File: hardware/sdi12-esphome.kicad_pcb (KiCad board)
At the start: 2 copper layers, 92.8 x 74 mm, 32 parts, among them J0 Grounding, J1 SDI-12 A, J2 SDI-12 B, J3 SDI-12 C, J4 SDI-12 D, J5 GPIO21/22, J6 Rain Gauge, Q1 2N7002, U1 ESP32_NODEMCU, U2 74LVC1G125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

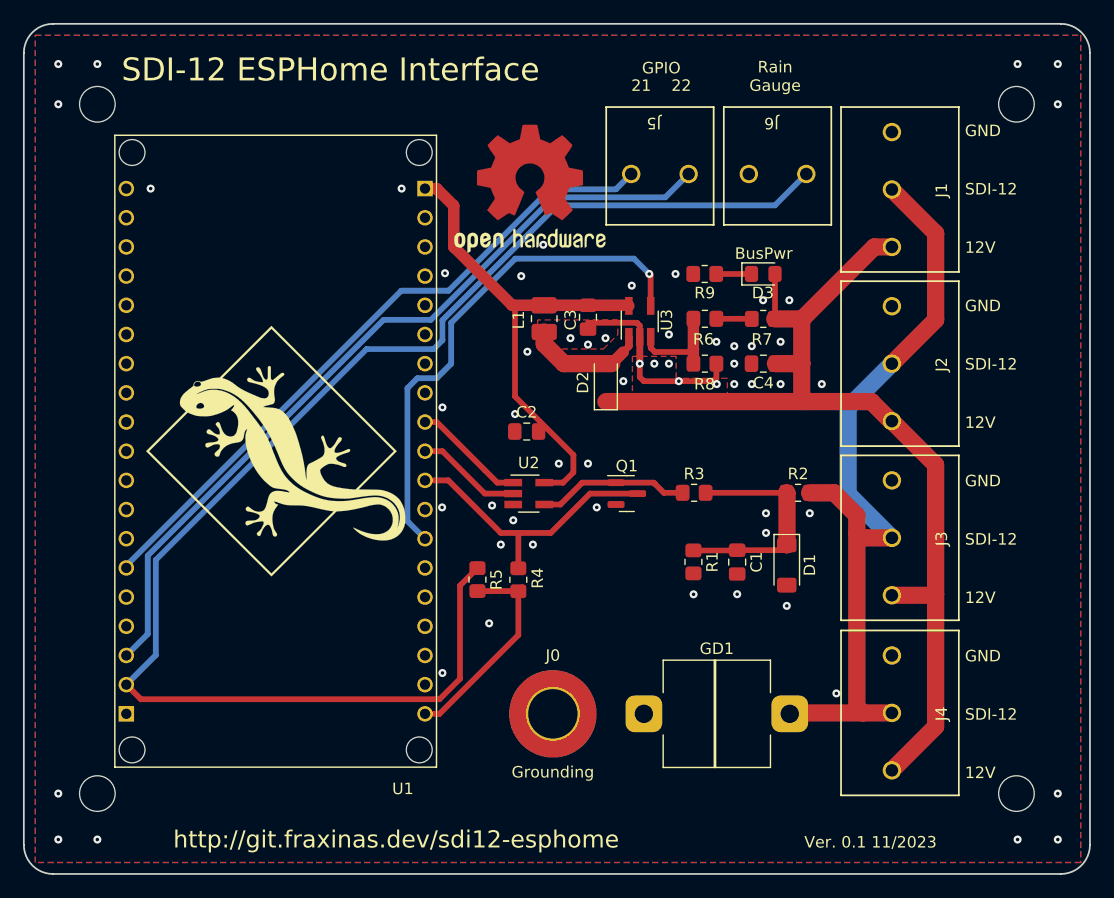
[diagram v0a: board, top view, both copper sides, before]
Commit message: board: Fix DRC errors (trace min spacing undercuts)
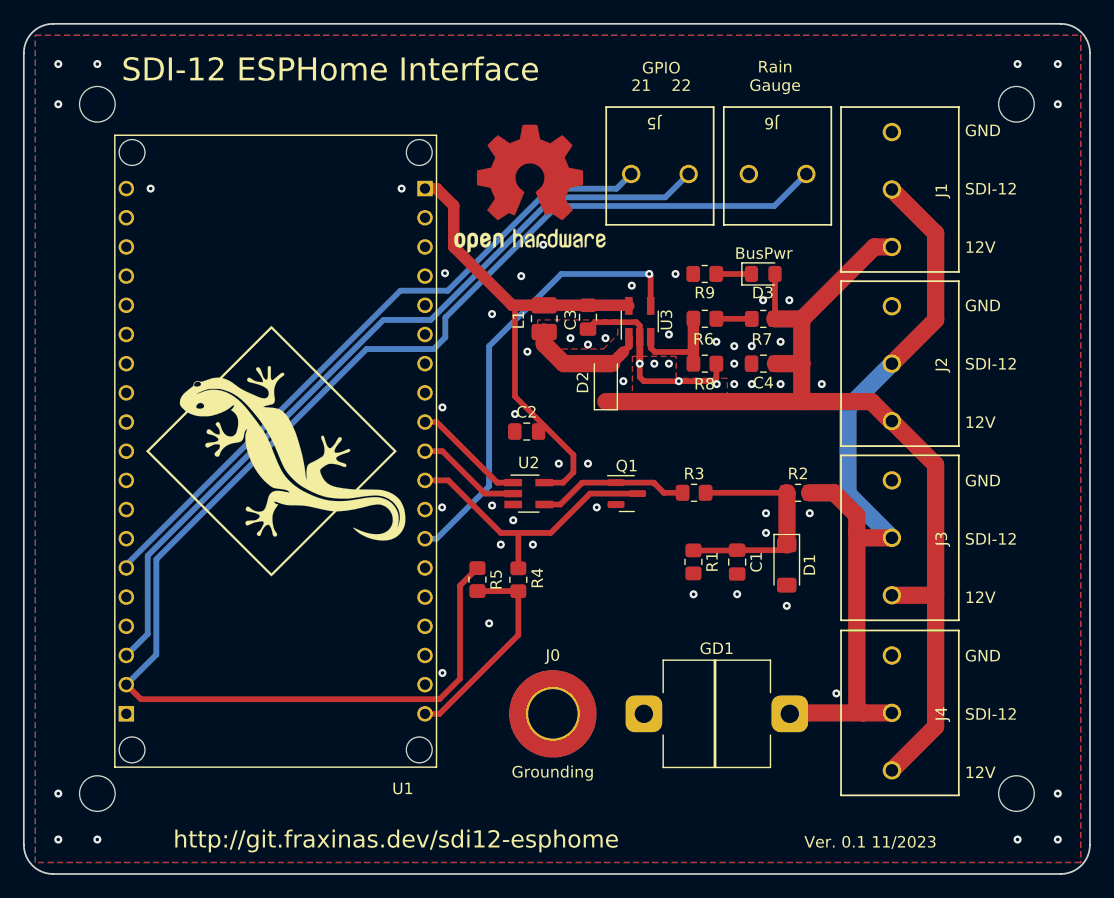
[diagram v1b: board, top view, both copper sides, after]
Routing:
- net VCC Enable: track 44.9 -> 39.0 mm
- net GND: track 17.8 -> 17.6 mm, vias 60 -> 61

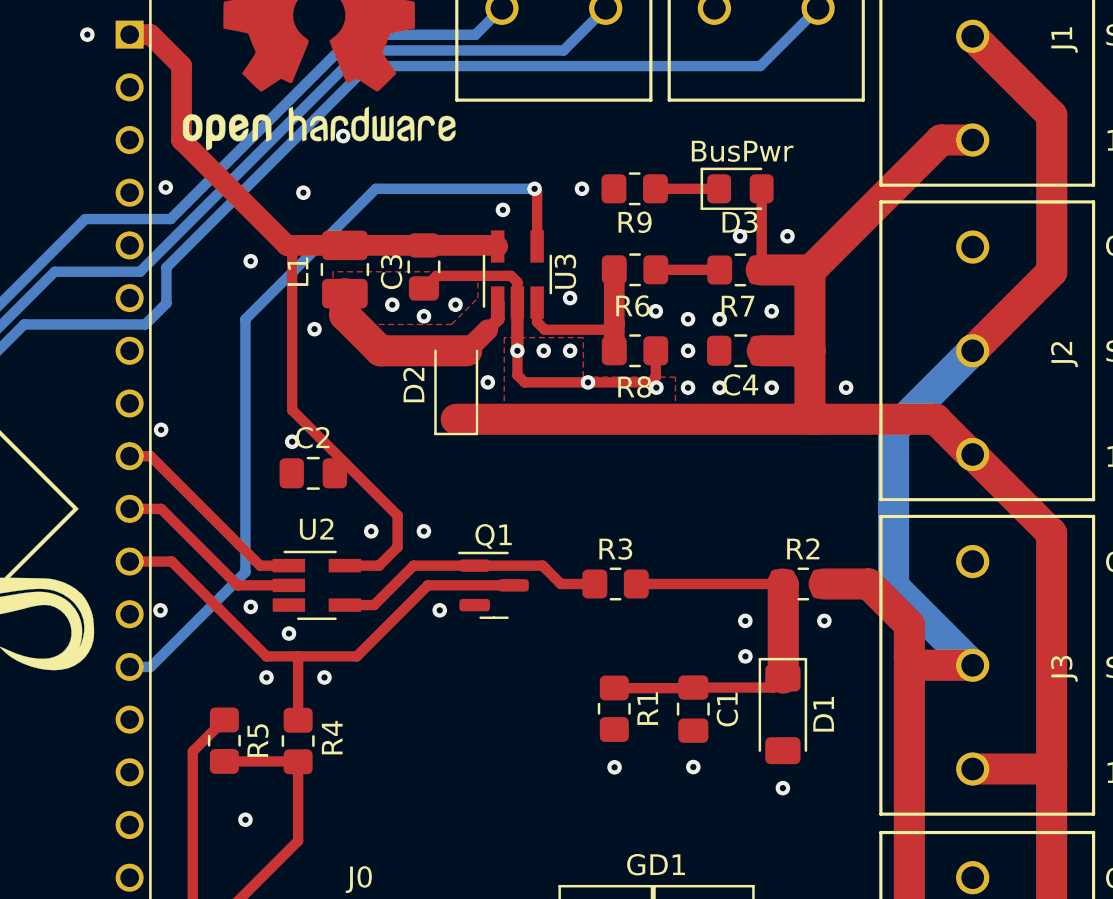
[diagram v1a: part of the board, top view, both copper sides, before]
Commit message: Board: Layout for power cut-off MOSFET
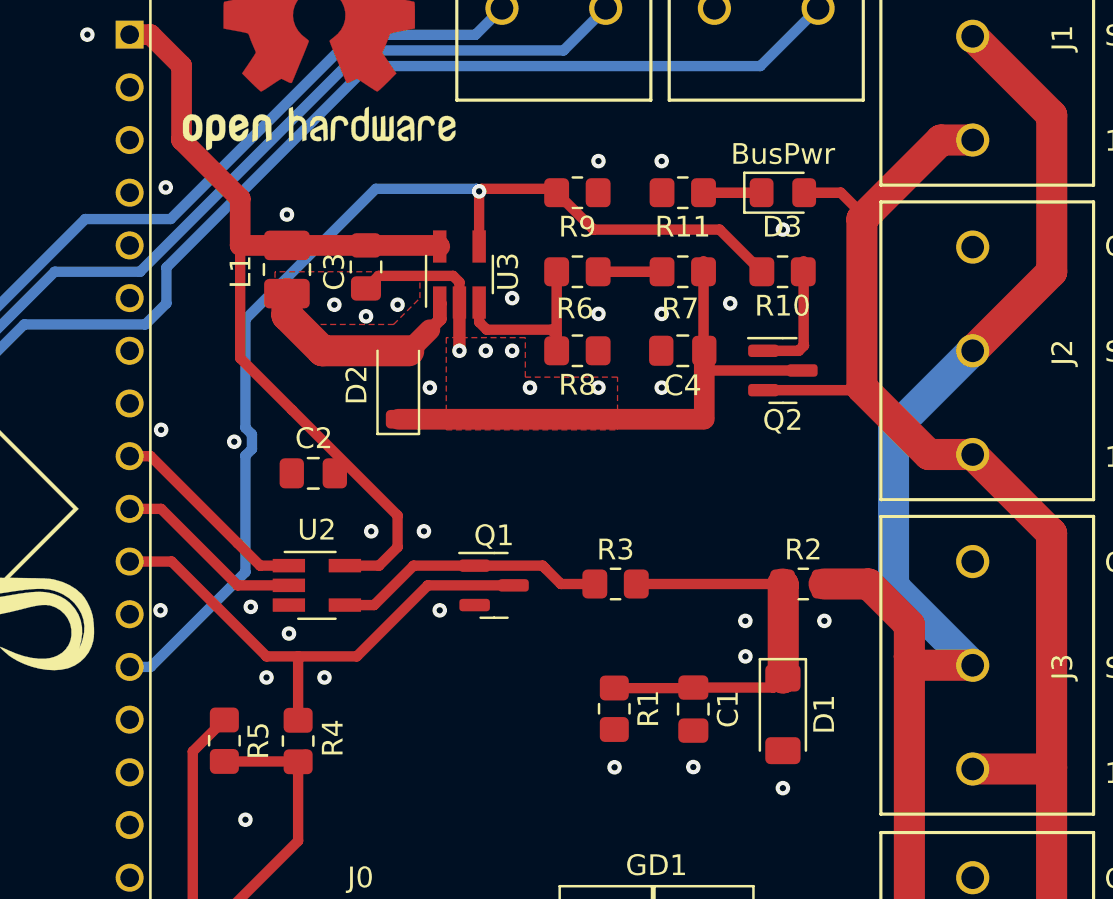
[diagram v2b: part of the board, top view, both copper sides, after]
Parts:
- added Q2: AO3401A, Package_TO_SOT_SMD:SOT-23, F.Cu at (105.4, 69.5)
- added R10: 10k, Resistor_SMD:R_0805_2012Metric_Pad1.20x1.40mm_HandSolder, F.Cu at (105.4, 64.8)
- added R11: 510R, Resistor_SMD:R_0805_2012Metric_Pad1.20x1.40mm_HandSolder, F.Cu at (100.6, 61.0)
- R9: value 510R -> 10k
- moved D2 2.79 mm to (86.9, 70.2)
- moved L1 2.79 mm to (81.5, 64.7)
- moved C3 2.79 mm to (85.3, 64.5)
- moved C4 2.79 mm to (100.6, 68.6)
- moved U3 2.79 mm to (89.8, 64.9)
- moved R6 2.78 mm to (95.5, 64.8)
- moved R7 2.78 mm to (100.6, 64.8)
- moved R8 2.78 mm to (95.5, 68.6)
- moved R9 2.77 mm to (95.5, 61.0)
- moved D3 2.06 mm to (105.4, 61.0)
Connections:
- C4 pad 1: +12V -> Net-(D2-K)
- D2 pad 1: +12V -> Net-(D2-K)
- R7 pad 1: +12V -> Net-(D2-K)
- R9 pad 1: GND -> VCC Enable
- R9 pad 2: Net-(D3-K) -> GND
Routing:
- net Net-(D2-K): track 0.00 -> 27.1 mm
- net +12V: track 89.3 -> 67.4 mm
- net VCC Enable: track 39.0 -> 51.8 mm
- net GND: track 17.6 -> 8.19 mm, vias 61 -> 52
- net Net-(Q2-G): track 0.00 -> 6.13 mm
- net Net-(D3-K): track 3.07 -> 2.29 mm
- net Net-(U3-V_{FB}): track 8.94 -> 9.71 mm
- net +5V: track 43.7 -> 43.2 mm

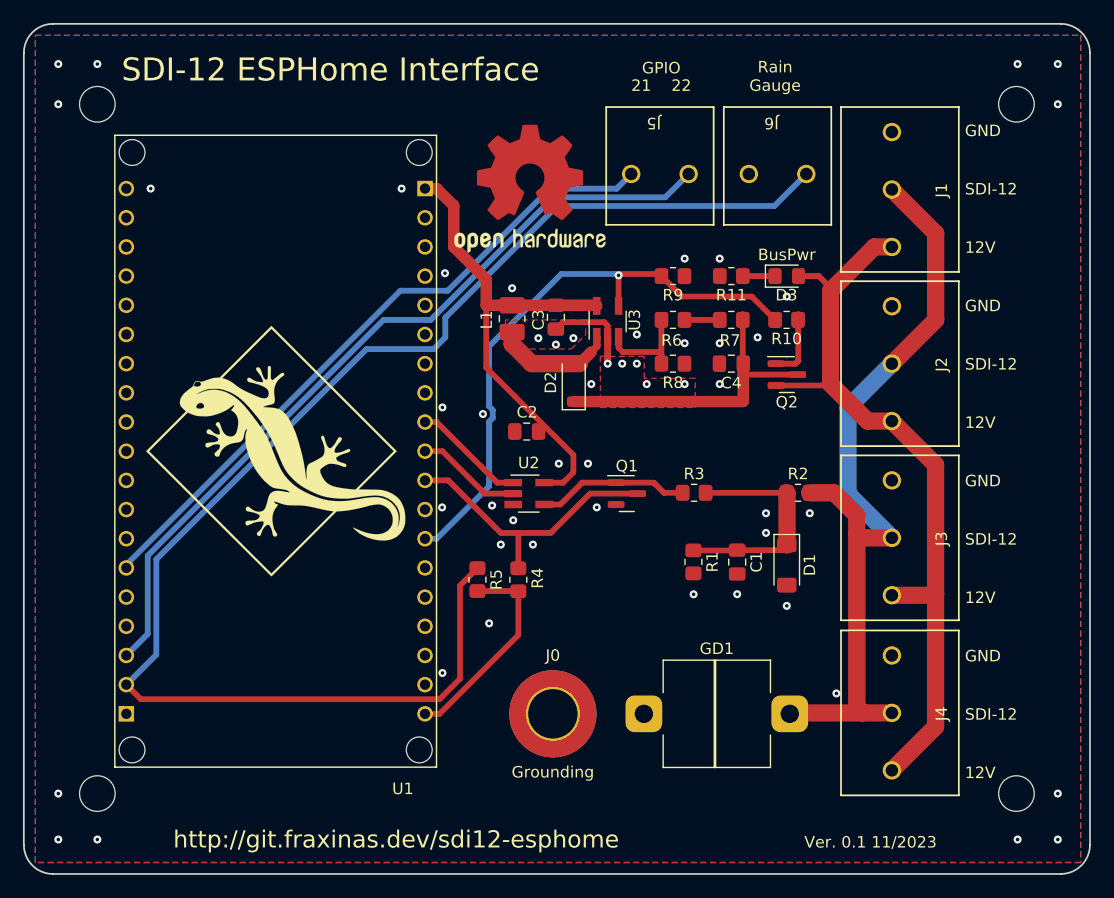
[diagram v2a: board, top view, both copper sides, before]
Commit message: Add Header for RCWL-1655 Distance Sensor Module
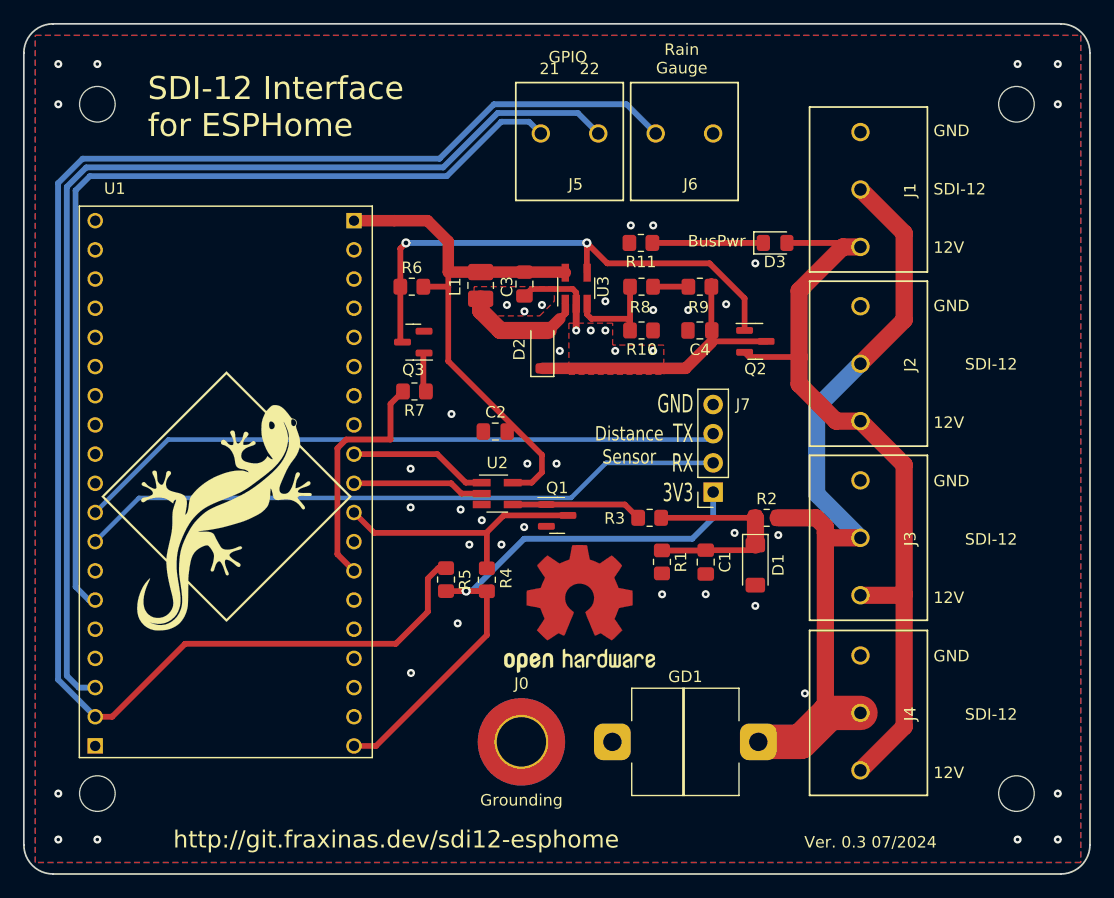
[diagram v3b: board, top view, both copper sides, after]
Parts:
- removed the R10 at (105.4, 64.8)
- removed the R9 at (95.5, 61.0)
- added J7: UART, Connector_PinSocket_2.54mm:PinSocket_1x04_P2.54mm_Vertical, F.Cu at (99.0, 79.8)
- added Q3: S8050, Package_TO_SOT_SMD:SOT-23, F.Cu at (72.9, 66.7)
- added R6: 12k, Resistor_SMD:R_0805_2012Metric_Pad1.20x1.40mm_HandSolder, F.Cu at (72.8, 61.9)
- added R7: 1k, Resistor_SMD:R_0805_2012Metric_Pad1.20x1.40mm_HandSolder, F.Cu at (73.0, 71.0)
- moved LOGO1 36.8 mm to (87.4, 89.9)
- moved J6 13.6 mm to (94.0, 48.5), turned to 0 degrees
- moved J5 13.3 mm to (84.0, 48.5), turned to 0 degrees
- moved R11 8.39 mm to (92.7, 58.1)
- moved Q1 6.35 mm to (85.4, 81.8)
- moved U1 6.28 mm to (55.3, 79.0), turned to 0 degrees
- moved G*** 6.08 mm to (56.6, 80.5), turned to -90 degrees
- moved R3 4.44 mm to (93.5, 82.0)
- moved R10 3.98 mm to (92.8, 65.7)
- moved R8 3.98 mm to (92.8, 61.9)
- moved C4 3.98 mm to (97.8, 65.7)
- moved D2 3.98 mm to (84.1, 67.3)
- moved Q2 3.98 mm to (102.7, 66.6)
- moved U3 3.98 mm to (87.1, 62.0)
- moved C3 3.98 mm to (82.6, 61.6)
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- renumbered R8 to R10, R6 to R8, R7 to R9
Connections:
- net RXD renamed SDI12_RXD
- net TXD renamed SDI12_TXD
- J5 pad 1: GPIO22 -> GPIO21
- J5 pad 2: GPIO21 -> GPIO22
- Q2 pad 1: Net-(Q2-G) -> BusPwr_{Enable}
- U1 pad J4_8: unconnected-(U1-G19-PadJ4_8) -> UART_TXD
- U1 pad J4_9: unconnected-(U1-G18-PadJ4_9) -> UART_RXD
- U1 pad J5_13: VCC Enable -> ~{BusPwr_{Enable}'}
- U3 pad 4: VCC Enable -> BusPwr_{Enable}
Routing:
- net UART_TXD: track 0.00 -> 56.6 mm
- net UART_RXD: track 0.00 -> 56.6 mm
- net VCC Enable: track 51.8 -> 0.00 mm, vias 1 -> 0
- net BusPwr_{Enable}: track 0.00 -> 45.8 mm, vias 0 -> 2
- net +3V3: track 19.0 -> 49.5 mm, vias 0 -> 1
- net GPIO22: track 70.3 -> 95.1 mm
- net GPIO21: track 58.3 -> 80.1 mm
- net ~{BusPwr_{Enable}'}: track 0.00 -> 20.8 mm
- net GPIO23: track 124.0 -> 141.3 mm
- net Net-(D3-K): track 2.29 -> 9.27 mm
- net Net-(Q2-G): track 6.13 -> 0.00 mm
- net +5V: track 43.2 -> 47.7 mm
- net Net-(Q3-B): track 0.00 -> 3.47 mm
- net +12V: track 67.4 -> 70.6 mm
- net Net-(D2-K): track 27.1 -> 24.6 mm
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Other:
- board text added: "Distance Sensor"
- board text added: "GND TX RX 3V3"
- board text added: "SDI-12 Interface for ESPHome"
- board text added: "Ver. 0.3 07/2024"
- board text removed: "SDI-12 ESPHome Interface"
- board text removed: "Ver. 0.1 11/2023"
